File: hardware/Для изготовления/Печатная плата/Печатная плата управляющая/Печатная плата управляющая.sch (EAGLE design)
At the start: 21 parts, among them IC2 LM317MABT, J1 POWER_JACK, X1 0446200001, X2 0446200001, X3 0446200001, X4 0446200001, X5 0446200001, X6 0446200001, X7 0446200001

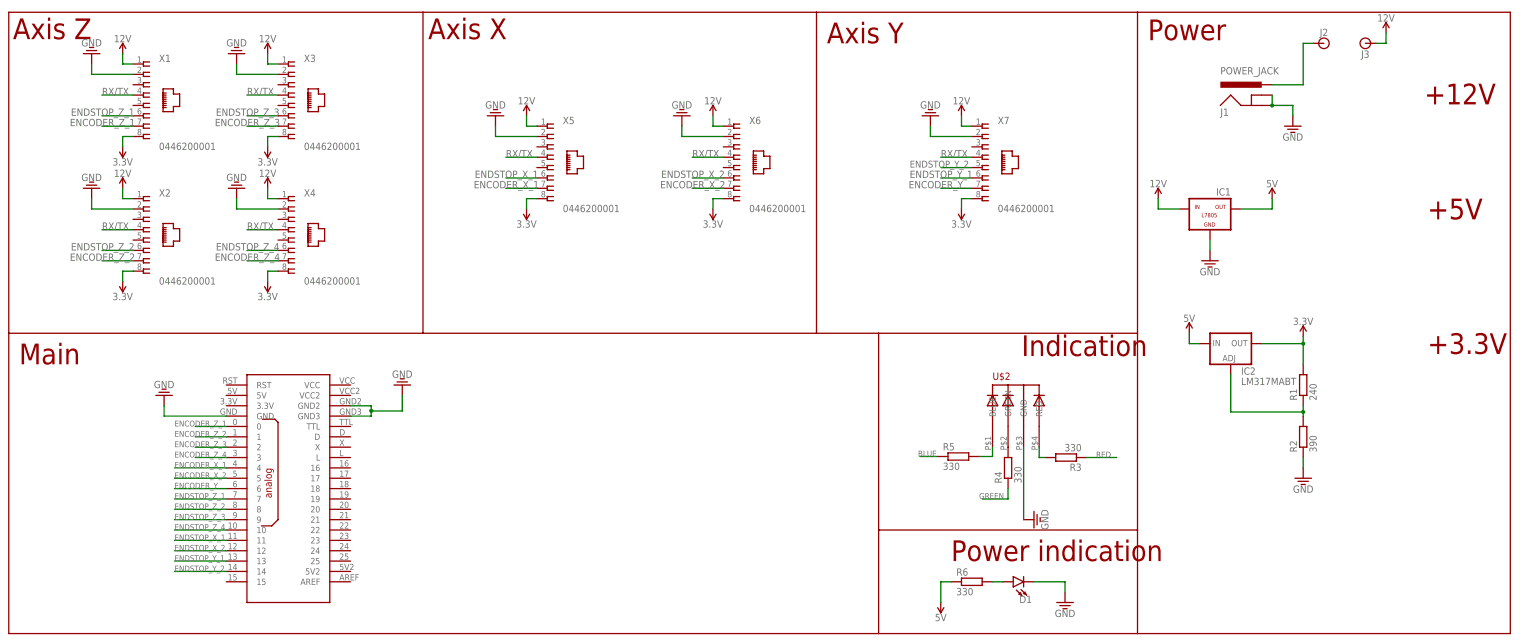
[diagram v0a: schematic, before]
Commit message: Добавлен клапан впускной
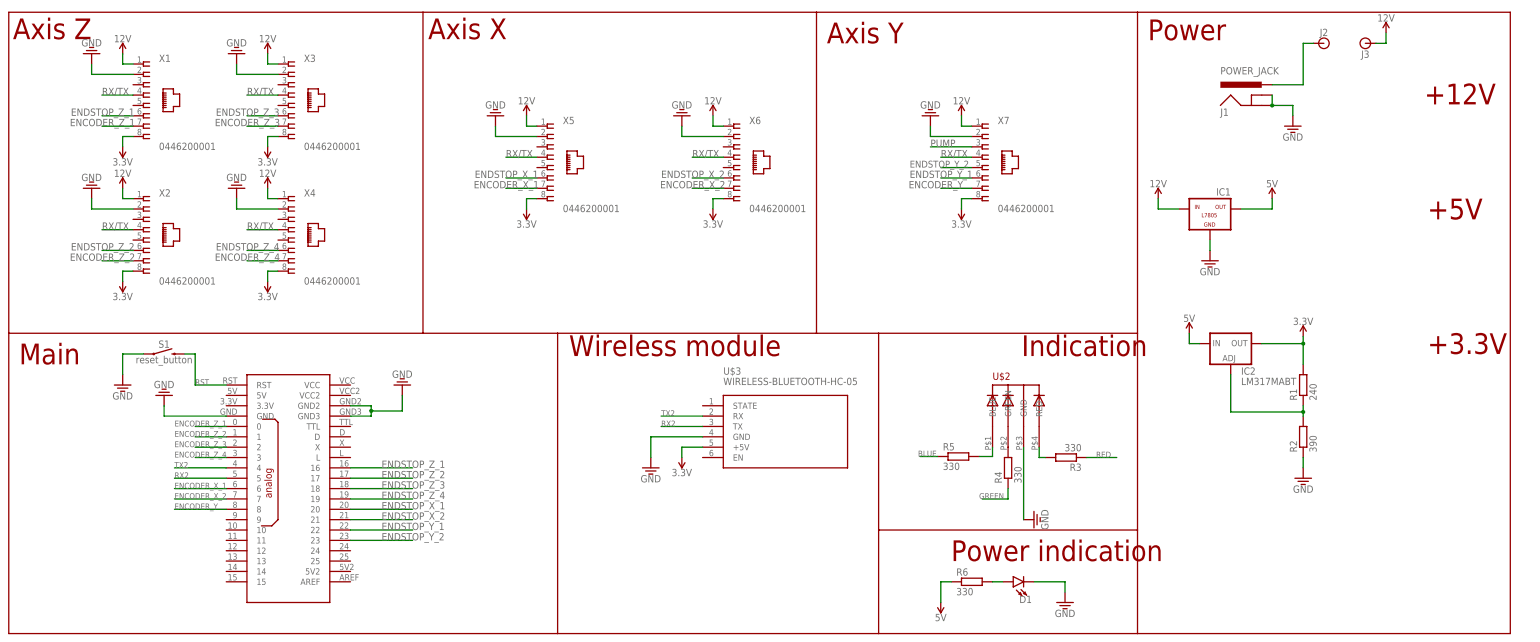
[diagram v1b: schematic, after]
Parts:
- added S1: reset_button, SparkFun-Switches:MOMENTARY-SWITCH-SPST-PTH-6.0MM
- added U$3: WIRELESS-BLUETOOTH-HC-05, diy-modules:WIRELESS-BLUETOOTH-HC-05
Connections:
- new net PUMP: X7.3
- new net RST: S1.2, U$1.RST
- new net RX2: U$1.5, U$3.TX
- new net TX2: U$1.4, U$3.RX
- net 3.3V: now also U$3.+5V
- net ENCODER_X_1: now also U$1.6; no longer U$1.4
- net ENCODER_X_2: now also U$1.7; no longer U$1.5
- net ENCODER_Y: now also U$1.8; no longer U$1.6
- net ENDSTOP_X_1: now also U$1.20; no longer U$1.11
- net ENDSTOP_X_2: now also U$1.21; no longer U$1.12
- net ENDSTOP_Y_1: now also U$1.22; no longer U$1.13
- net ENDSTOP_Y_2: now also U$1.23; no longer U$1.14
- net ENDSTOP_Z_1: now also U$1.16; no longer U$1.7
- net ENDSTOP_Z_2: now also U$1.17; no longer U$1.8
- net ENDSTOP_Z_3: now also U$1.18; no longer U$1.9
- net ENDSTOP_Z_4: now also U$1.19; no longer U$1.10
- net GND: now also S1.1, U$3.GND
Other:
- note added: "Wireless module"

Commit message: изменена управляющая плата
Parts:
- removed X1, X2, X3, X4, X5, X6, X7: 0446200001, con-molex:0446200001
- added J10, J4, J5, J6, J7, J8, J9: (no value), Wurth_Elektronik_Electromechanic_Input-Output_Connectors_rev16a:615006138421
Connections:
- new net ENDSTOP_Y: J6.5
- net 12V: now also J10.2, J4.2, J5.2, J6.2, J7.2, J8.2, J9.2, U$1.VCC, U$1.VCC2; no longer X1.1, X2.1, X3.1, X4.1, X5.1, X6.1, X7.1
- net 3.3V: now also J10.3, J4.3, J5.3, J6.3, J7.3, J8.3, J9.3; no longer X1.8, X2.8, X3.8, X4.8, X5.8, X6.8, X7.8
- net ENCODER_X_1: now also J4.6, J8.6; no longer X5.7
- net ENCODER_X_2: now also J5.6; no longer X6.7
- net ENCODER_Y: now also J6.6; no longer X7.7
- net ENCODER_Z_1: now also J7.6; no longer X1.7
- net ENCODER_Z_2: no longer X2.7
- net ENCODER_Z_3: now also J10.6; no longer X3.7
- net ENCODER_Z_4: now also J9.6; no longer X4.7
- net ENDSTOP_X_1: now also J4.5; no longer X5.6
- net ENDSTOP_X_2: now also J5.5; no longer X6.6
- net ENDSTOP_Y_1: no longer X7.6
- net ENDSTOP_Y_2: no longer X7.5
- net ENDSTOP_Z_1: now also J7.5; no longer X1.6
- net ENDSTOP_Z_2: now also J8.5; no longer X2.6
- net ENDSTOP_Z_3: now also J10.5; no longer X3.6
- net ENDSTOP_Z_4: now also J9.5; no longer X4.6
- net GND: now also J10.4, J4.4, J5.4, J6.4, J7.4, J8.4, J9.4; no longer X1.2, X2.2, X3.2, X4.2, X5.2, X6.2, X7.2
- net PUMP: now also U$1.24; no longer X7.3
- net RX/TX: now also J10.1, J4.1, J5.1, J6.1, J7.1, J8.1, J9.1, U$1.TTL; no longer X1.4, X2.4, X3.4, X4.4, X5.4, X6.4, X7.4

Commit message: изменена управляющая плата
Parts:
- removed IC1: (no value), tango:L7805
- removed IC2: LM317MABT, v-reg:LM317MABT
- removed R2: 390, resistor:R-EU_0204/7
- added J11, J12: (no value), SparkFun-Connectors:BANANA_CONN
- added Q1: IRF540, transistor-power:IRF540
- R1: value 240 -> 330
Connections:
- removed net ENDSTOP_Y_1: U$1.22
- removed net ENDSTOP_Y_2: U$1.23
- net 12V: now also Q1.S; no longer IC1.IN
- net 3.3V: now also U$1.3.3V; no longer IC2.OUT, R1.2
- net 5V: now also U$1.5V, U$1.5V2; no longer IC1.OUT, IC2.IN
- net BLUE: now also U$1.16
- net ENCODER_X_1: now also U$1.10; no longer J8.6, U$1.6
- net ENCODER_X_2: now also U$1.14; no longer U$1.7
- net ENCODER_Y: now also U$1.24; no longer U$1.8
- net ENCODER_Z_2: now also J8.6, U$1.2; no longer U$1.1
- net ENCODER_Z_3: now also U$1.6; no longer U$1.2
- net ENCODER_Z_4: now also U$1.8; no longer U$1.3
- net ENDSTOP_X_1: now also U$1.13; no longer U$1.20
- net ENDSTOP_X_2: now also U$1.15; no longer U$1.21
- net ENDSTOP_Y: now also U$1.25
- net ENDSTOP_Z_1: now also U$1.1; no longer U$1.16
- net ENDSTOP_Z_2: now also U$1.3; no longer U$1.17
- net ENDSTOP_Z_3: now also U$1.7; no longer U$1.18
- net ENDSTOP_Z_4: now also U$1.9; no longer U$1.19
- net GND: now also J12.1, U$1.GND2, U$1.GND3; no longer IC1.GND, R2.1
- net GREEN: now also U$1.17
- net N$1: now also J11.1, Q1.D; no longer U$1.GND2, U$1.GND3
- net N$3: now also Q1.G; no longer IC2.ADJ, R2.2
- net PUMP: now also R1.2, U$1.19; no longer U$1.24
- net RED: now also U$1.18
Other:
- note removed: "+3.3V"
- note removed: "+5V"
- moved on the sheet: R1

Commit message: изменена управляющая плата
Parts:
- removed S1: reset_button, SparkFun-Switches:MOMENTARY-SWITCH-SPST-PTH-6.0MM
- R1: value 330 -> 100
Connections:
- removed net RST: S1.2, U$1.RST
- net BLUE: now also U$1.13; no longer U$1.16
- net ENCODER_X_1: now also U$1.20; no longer U$1.10
- net ENCODER_X_2: now also U$1.22; no longer U$1.14
- net ENDSTOP_X_1: now also U$1.19; no longer U$1.13
- net ENDSTOP_X_2: now also U$1.21; no longer U$1.15
- net ENDSTOP_Y: now also U$1.23; no longer U$1.25
- net GND: no longer S1.1
- net GREEN: now also U$1.14; no longer U$1.17
- net PUMP: now also U$1.25; no longer U$1.19
- net RED: now also U$1.15; no longer U$1.18
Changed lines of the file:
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@@
 <part name="GND15" library="SparkFun-PowerSymbols" deviceset="GND2" device="" value="GND"/>
 <part name="SUPPLY15" library="SparkFun-PowerSymbols" deviceset="3.3V" device=""/>
-<part name="S1" library="SparkFun-Switches" deviceset="MOMENTARY-SWITCH-SPST" device="-PTH-6.0MM" value="reset_button"/>
-<part name="GND16" library="SparkFun-PowerSymbols" deviceset="GND2" device="" value="GND"/>
 <part name="SUPPLY22" library="SparkFun-PowerSymbols" deviceset="12V" device=""/>
 <part name="SUPPLY13" library="SparkFun-PowerSymbols" deviceset="3.3V" device=""/>
@@
 <part name="GND9" library="SparkFun-PowerSymbols" deviceset="GND2" device="" value="GND"/>
 <part name="J12" library="SparkFun-Connectors" deviceset="BANANA_CONN" device=""/>
-<part name="R1" library="resistor" library_urn="urn:adsk.eagle:library:348" deviceset="R-EU_" device="0204/7" package3d_urn="urn:adsk.eagle:package:25945/1" value="330"/>
+<part name="R1" library="resistor" library_urn="urn:adsk.eagle:library:348" deviceset="R-EU_" device="0204/7" package3d_urn="urn:adsk.eagle:package:25945/1" value="100"/>
 </parts>
 <sheets>
@@
 <instance part="GND15" gate="GND" x="289.56" y="48.26"/>
 <instance part="SUPPLY15" gate="G$1" x="297.18" y="50.8" rot="R180"/>
-<instance part="S1" gate="G$1" x="170.18" y="76.2"/>
-<instance part="GND16" gate="GND" x="160.02" y="68.58"/>
 <instance part="SUPPLY22" gate="G$1" x="220.98" y="73.66"/>
 <instance part="SUPPLY13" gate="G$1" x="353.06" y="121.92"/>
@@
 <instance part="GND12" gate="GND" x="228.6" y="68.58" rot="R180"/>
 <instance part="SUPPLY16" gate="G$1" x="175.26" y="66.04"/>
-<instance part="SUPPLY17" gate="G$1" x="180.34" y="66.04" rot="R90"/>
+<instance part="SUPPLY17" gate="G$1" x="182.88" y="66.04" rot="R90"/>
 <instance part="SUPPLY18" gate="G$1" x="220.98" y="22.86" rot="R270"/>
 <instance part="Q1" gate="G$1" x="439.42" y="60.96"/>
@@
 </segment>
 <segment>
-<pinref part="GND16" gate="GND" pin="GND"/>
-<wire x1="160.02" y1="71.12" x2="160.02" y2="76.2" width="0.1524" layer="91"/>
-<pinref part="S1" gate="G$1" pin="1"/>
-<wire x1="160.02" y1="76.2" x2="165.1" y2="76.2" width="0.1524" layer="91"/>
-</segment>
-<segment>
 <pinref part="GND7" gate="GND" pin="GND"/>
 <pinref part="J6" gate="G$1" pin="4"/>
@@
 </segment>
 <segment>
-<pinref part="U$1" gate="G$1" pin="13"/>
-<wire x1="185.42" y1="25.4" x2="177.8" y2="25.4" width="0.1524" layer="91"/>
-<wire x1="175.26" y1="25.4" x2="172.72" y2="25.4" width="0.1524" layer="91"/>
-<wire x1="177.8" y1="25.4" x2="175.26" y2="25.4" width="0.1524" layer="91"/>
-<label x="172.72" y="25.4" size="1.4224" layer="95"/>
+<wire x1="233.68" y1="40.64" x2="215.9" y2="40.64" width="0.1524" layer="91"/>
+<label x="220.98" y="40.64" size="1.4224" layer="95"/>
+<pinref part="U$1" gate="G$1" pin="19"/>
 </segment>
 </net>
@@
 </segment>
 <segment>
-<pinref part="U$1" gate="G$1" pin="10"/>
-<wire x1="185.42" y1="33.02" x2="172.72" y2="33.02" width="0.1524" layer="91"/>
-<label x="172.72" y="33.02" size="1.4224" layer="95"/>
+<wire x1="233.68" y1="38.1" x2="215.9" y2="38.1" width="0.1524" layer="91"/>
+<label x="220.98" y="38.1" size="1.4224" layer="95"/>
+<pinref part="U$1" gate="G$1" pin="20"/>
 </segment>
 </net>
@@
 </segment>
 <segment>
-<pinref part="U$1" gate="G$1" pin="15"/>
-<wire x1="185.42" y1="20.32" x2="172.72" y2="20.32" width="0.1524" layer="91"/>
-<label x="172.72" y="20.32" size="1.4224" layer="95"/>
+<wire x1="233.68" y1="35.56" x2="215.9" y2="35.56" width="0.1524" layer="91"/>
+<label x="220.98" y="35.56" size="1.4224" layer="95"/>
+<pinref part="U$1" gate="G$1" pin="21"/>
 </segment>
 </net>
@@
 </segment>
 <segment>
-<pinref part="U$1" gate="G$1" pin="14"/>
-<wire x1="185.42" y1="22.86" x2="172.72" y2="22.86" width="0.1524" layer="91"/>
-<label x="172.72" y="22.86" size="1.4224" layer="95"/>
+<wire x1="233.68" y1="33.02" x2="215.9" y2="33.02" width="0.1524" layer="91"/>
+<label x="220.98" y="33.02" size="1.4224" layer="95"/>
+<pinref part="U$1" gate="G$1" pin="22"/>
 </segment>
 </net>
@@
 </segment>
 <segment>
+<wire x1="215.9" y1="27.94" x2="226.06" y2="27.94" width="0.1524" layer="91"/>
+<label x="220.98" y="27.94" size="1.4224" layer="95"/>
 <pinref part="U$1" gate="G$1" pin="24"/>
-<wire x1="215.9" y1="27.94" x2="223.52" y2="27.94" width="0.1524" layer="91"/>
-<label x="218.44" y="27.94" size="1.4224" layer="95"/>
 </segment>
 </net>
@@
 <pinref part="SUPPLY17" gate="G$1" pin="5V"/>
 <pinref part="U$1" gate="G$1" pin="5V"/>
-<wire x1="180.34" y1="66.04" x2="185.42" y2="66.04" width="0.1524" layer="91"/>
+<wire x1="182.88" y1="66.04" x2="185.42" y2="66.04" width="0.1524" layer="91"/>
 </segment>
 <segment>
@@
 </segment>
 <segment>
-<pinref part="U$1" gate="G$1" pin="16"/>
-<wire x1="215.9" y1="48.26" x2="220.98" y2="48.26" width="0.1524" layer="91"/>
-<label x="218.44" y="48.26" size="1.4224" layer="95"/>
+<label x="177.8" y="25.4" size="1.4224" layer="95"/>
+<pinref part="U$1" gate="G$1" pin="13"/>
+<wire x1="185.42" y1="25.4" x2="175.26" y2="25.4" width="0.1524" layer="91"/>
 </segment>
 </net>
@@
 </segment>
 <segment>
-<pinref part="U$1" gate="G$1" pin="17"/>
-<wire x1="215.9" y1="45.72" x2="220.98" y2="45.72" width="0.1524" layer="91"/>
-<label x="218.44" y="45.72" size="1.4224" layer="95"/>
+<label x="177.8" y="22.86" size="1.4224" layer="95"/>
+<pinref part="U$1" gate="G$1" pin="14"/>
+<wire x1="175.26" y1="22.86" x2="185.42" y2="22.86" width="0.1524" layer="91"/>
 </segment>
 </net>
@@
 </segment>
 <segment>
-<pinref part="U$1" gate="G$1" pin="18"/>
-<wire x1="215.9" y1="43.18" x2="220.98" y2="43.18" width="0.1524" layer="91"/>
-<label x="218.44" y="43.18" size="1.4224" layer="95"/>
+<label x="177.8" y="20.32" size="1.4224" layer="95"/>
+<pinref part="U$1" gate="G$1" pin="15"/>
+<wire x1="175.26" y1="20.32" x2="185.42" y2="20.32" width="0.1524" layer="91"/>
 </segment>
 </net>
@@
 </segment>
 </net>
-<net name="RST" class="0">
-<segment>
-<pinref part="U$1" gate="G$1" pin="RST"/>
-<wire x1="185.42" y1="68.58" x2="177.8" y2="68.58" width="0.1524" layer="91"/>
-<label x="177.8" y="68.58" size="1.4224" layer="95"/>
-<pinref part="S1" gate="G$1" pin="2"/>
-<wire x1="175.26" y1="76.2" x2="177.8" y2="76.2" width="0.1524" layer="91"/>
-<wire x1="177.8" y1="76.2" x2="177.8" y2="68.58" width="0.1524" layer="91"/>
-</segment>
-</net>
 <net name="ENDSTOP_Y" class="0">
 <segment>
@@
 </segment>
 <segment>
-<pinref part="U$1" gate="G$1" pin="25"/>
-<wire x1="215.9" y1="25.4" x2="223.52" y2="25.4" width="0.1524" layer="91"/>
-<label x="218.44" y="25.4" size="1.4224" layer="95"/>
+<wire x1="215.9" y1="30.48" x2="226.06" y2="30.48" width="0.1524" layer="91"/>
+<label x="220.98" y="30.48" size="1.4224" layer="95"/>
+<pinref part="U$1" gate="G$1" pin="23"/>
 </segment>
 </net>
@@
 <net name="PUMP" class="0">
 <segment>
-<pinref part="U$1" gate="G$1" pin="19"/>
-<wire x1="215.9" y1="40.64" x2="223.52" y2="40.64" width="0.1524" layer="91"/>
-<label x="218.44" y="40.64" size="1.778" layer="95"/>
-</segment>
-<segment>
 <pinref part="R1" gate="G$1" pin="2"/>
 <wire x1="424.434" y1="58.42" x2="416.56" y2="58.42" width="0.1524" layer="91"/>
 <label x="416.56" y="58.42" size="1.778" layer="95"/>
 </segment>
-</net>
+<segment>
+<pinref part="U$1" gate="G$1" pin="25"/>
+<wire x1="215.9" y1="25.4" x2="226.06" y2="25.4" width="0.1524" layer="91"/>
+<label x="220.98" y="25.4" size="1.778" layer="95"/>
+</segment>
+</net>
